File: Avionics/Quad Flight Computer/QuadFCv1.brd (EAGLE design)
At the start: 49.5 x 49.5 mm, 121 parts, among them J2 1050270001, Q1 DMP2035U, Q2 DMP2035U, Q3 DMP2035U, SW1 2-1437565-9, U1 TM4C123GH6PZ, U10 LTC4412, U11 AP7215-33YG-13, U2 74LVC4245APW, U3 ATMEGA32U2-MU, U5 MPU-6000, U6 HMC5883LSMD, U7 MS5611-01BA, U8 74AUP1G19GW, U9 S25FL127S, X1 HWB, Y1 32.768KHZ, Y2 AWSCR-20.00CW-T, Y3 PRQC16.00SR5010X000

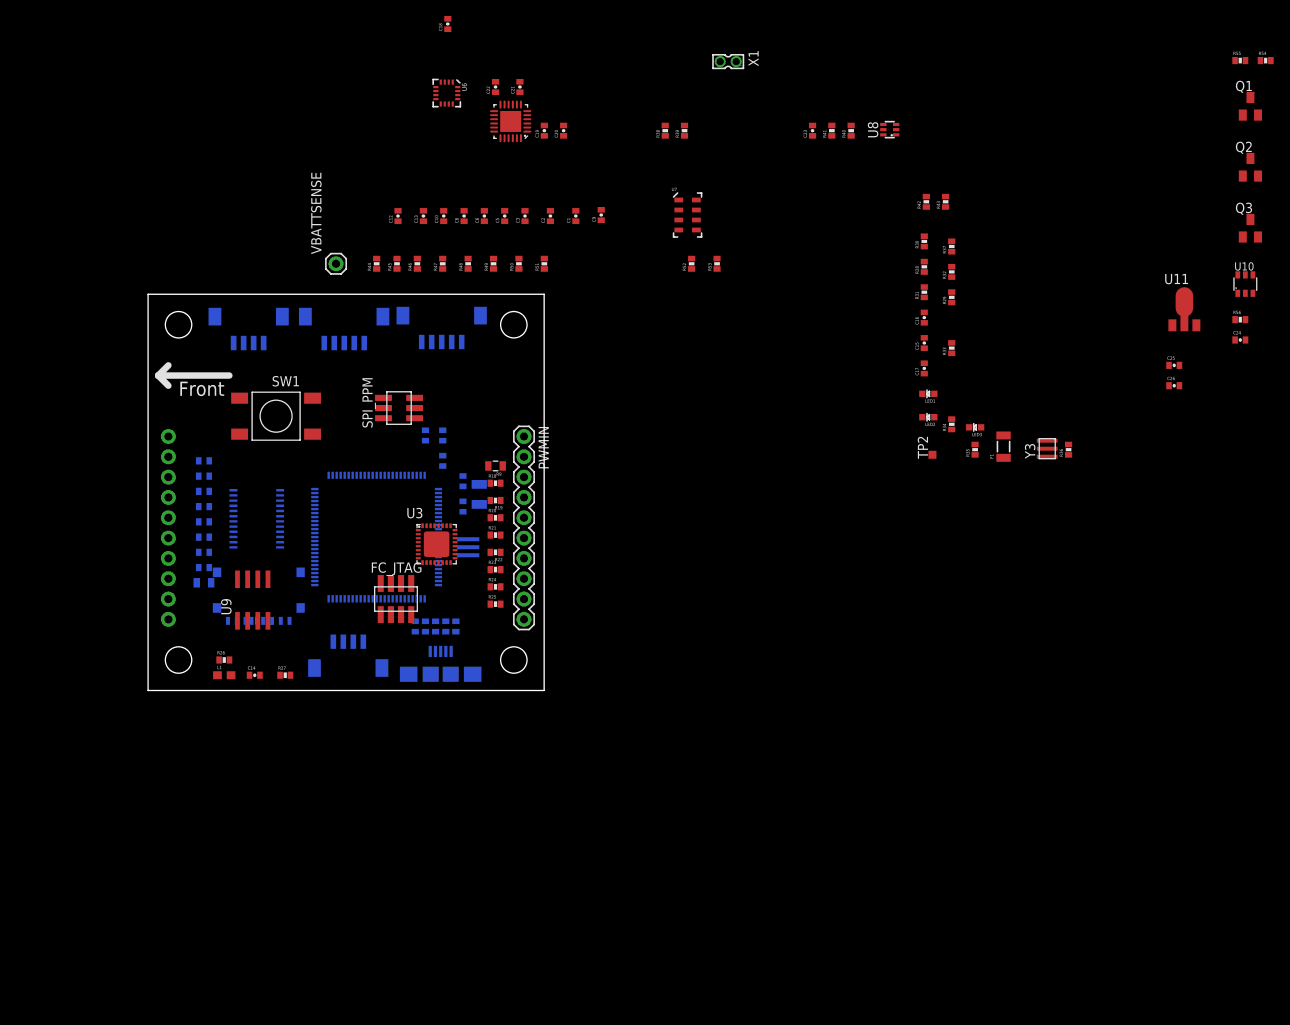
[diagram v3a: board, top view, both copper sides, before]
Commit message: Consolidated entire design into single FC library. Makes everything neater and avoids package conflicts. Using any new package should be added to this library OR copied to it from another lib.
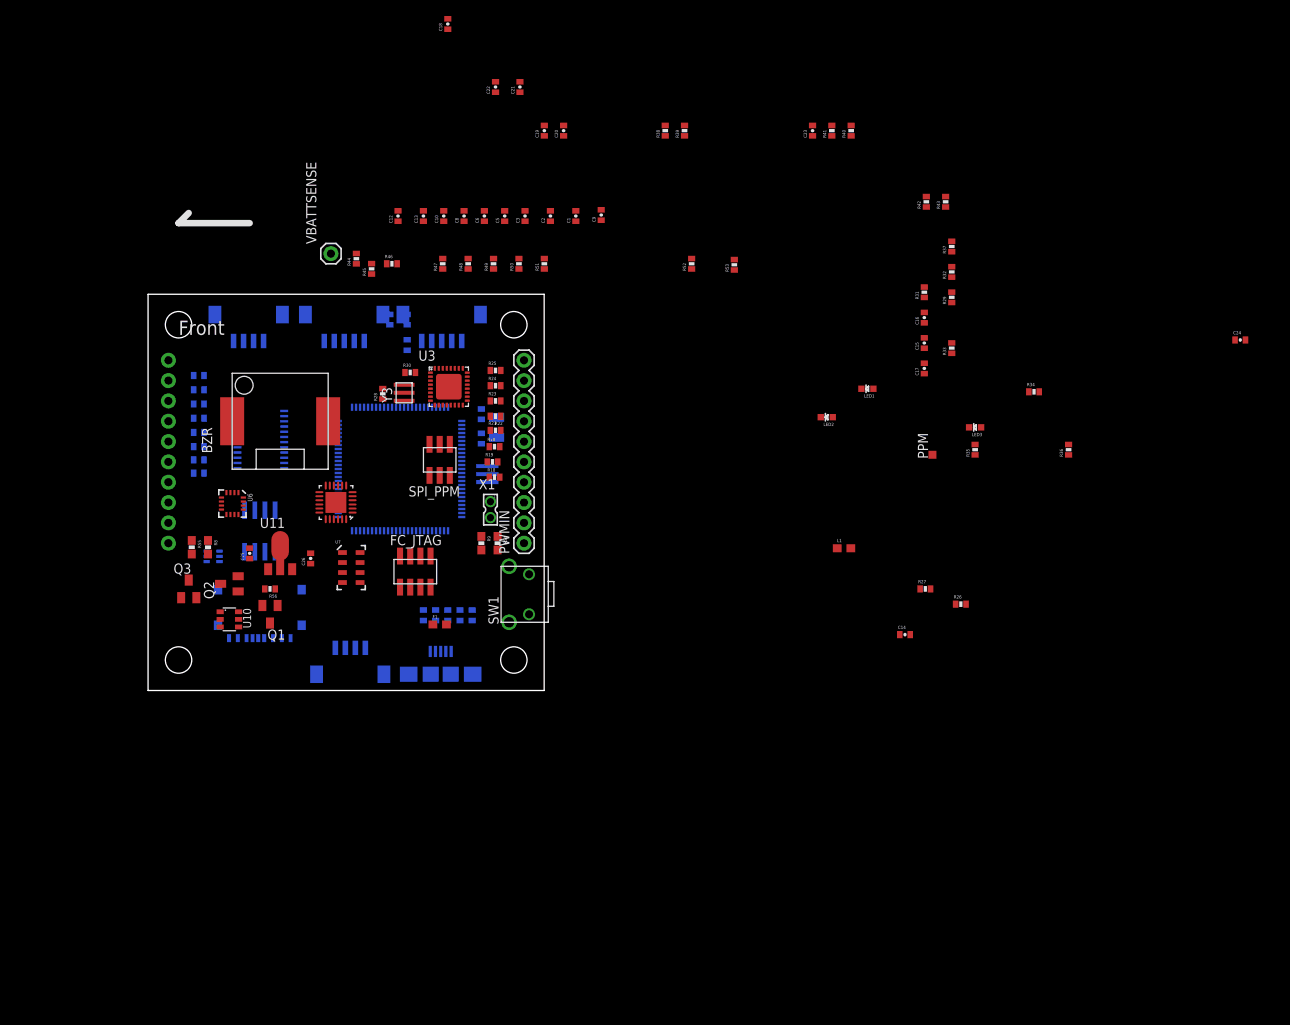
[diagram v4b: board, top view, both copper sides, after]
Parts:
- removed TP2: TPSQTP10SQ, testpad:TP10SQ
- added BZR: CMT-1203-SMT, QuadFCv1:CMT-1203-SMT
- added PPM: TESTPAD_TPSQTP10SQ, QuadFCv1:TP10SQ
- C1, C10, C11, C12, C13, C14, C15, C16, C17, C18, C19, C2, C20, C21, C22, C23, C24, C25, C26, C3, C4, C5, C6, C7, C8, C9: device SparkFun-Capacitors:0402-CAP -> QuadFCv1:0402-CAP
- F1: device SparkFun:PTC-1206 -> QuadFCv1:SPARKFUN_0603
- FC_JTAG: device Shared Libraries:2X4_SMT-0.05 -> QuadFCv1:2X4_SMT-0.05
- GPS, I2C: device Shared Libraries:DF13_4POS -> QuadFCv1:DF13_4POS
- ISENSE, RADIO1: device Shared Libraries:DF13_5POS -> QuadFCv1:DF13_5POS
- J2: device Shared Libraries:1050270001 -> QuadFCv1:1050270001
- L1: device SparkFun-Passives:0603 -> QuadFCv1:0603
- LED1, LED2, LED3: device SparkFun:LED-0603 -> QuadFCv1:SPARKFUN_LED-0603
- PWMIN, PWMOUT: device SparkFun-Connectors:1X10 -> QuadFCv1:1X10
- Q1, Q2, Q3: device Shared Libraries:SOT23 -> QuadFCv1:SOT23
- R1, R10, R11, R12, R13, R14, R15, R16, R17, R18, R19, R2, R20, R21, R22, R23, R24, R25, R26, R27, R28, R29, R3, R30, R31, R32, R33, R34, R35, R36, R37, R38, R39, R4, R40, R41, R42, R43, R44, R45, R46, R47, R48, R49, R5, R50, R51, R52, R53, R6, R7: device SparkFun-Resistors:0402-RES -> QuadFCv1:0402-RES
- R54, R55: device SparkFun-Resistors:0402-RES -> QuadFCv1:0603-RES
- R56: device Shared Libraries:0402-RES -> QuadFCv1:0402-RES
- R8, R9: device SparkFun-Resistors:0805 -> QuadFCv1:0603-RES
- SPI_PPM: device Shared Libraries:2X3_SMT_0.5 -> QuadFCv1:2X3_SMT_0.5
- STANDOFF1, STANDOFF2, STANDOFF3, STANDOFF4: device SparkFun-Electromechanical:STAND-OFF -> QuadFCv1:STAND-OFF
- SW1: value 2-1437565-9 -> PTS635VL31-VERT; device Shared Libraries:SMD_BUTTON_6X6 -> QuadFCv1:PTS635VL31
- U1: device Shared Libraries:LQFP100 -> QuadFCv1:LQFP100
- U10: device Shared Libraries:SOT23-6 -> QuadFCv1:SOT23-6
- U11: device Shared Libraries:SOT89 -> QuadFCv1:SOT89
- U12: device SparkFun-Connectors:USB-AB-MICRO-SMD -> QuadFCv1:USB-AB-MICRO-SMD
- U2: device Shared Libraries:TSSOP24 -> QuadFCv1:TSSOP24
- U3: device atmel:QFN32 -> QuadFCv1:QFN32
- U5: value MPU-6000 -> INVESENSE_MPU-6000; device Invesense:QFN-24-4MM2 -> QuadFCv1:QFN-24-4MM2
- U6: device Shared Libraries:16LPCC -> QuadFCv1:16LPCC
- U7: device 3DRobotics:MS5611-01BA -> QuadFCv1:MS5611-01BA
- U8: device Shared Libraries:SOT363_PHILIPS -> QuadFCv1:SOT363_PHILIPS
- U9: device Shared Libraries:SOIC8 -> QuadFCv1:SOIC8
- VBATTSENSE: device SparkFun-Connectors:1X01 -> QuadFCv1:1X01
- X1: device con-molex:87758-0216 -> QuadFCv1:87758-0216
- Y1: device Shared Libraries:ECS-.327-12.5-34B -> QuadFCv1:ECS-.327-12.5-34B
- Y2: device Shared Libraries:AWSCR-CW -> QuadFCv1:AWSCR-CW
- Y3: device Shared Libraries:PRQC16.00SR5010X000 -> QuadFCv1:PRQC16.00SR5010X000
- moved R55 144.5 mm to (5.46, 17.9), turned to 270 degrees
- moved Q3 140.2 mm to (5.08, 12.7)
- moved Q1 138.0 mm to (15.2, 9.53), turned to 180 degrees
- moved Q2 137.8 mm to (10.2, 13.3), turned to 90 degrees
- moved U10 133.7 mm to (10.2, 8.89), turned to 270 degrees
- moved R56 125.9 mm to (15.2, 12.7), turned to 180 degrees
- moved C25 117.9 mm to (12.7, 17.1), turned to 90 degrees
- moved U11 117.1 mm to (16.5, 17.1)
- moved R54 113.4 mm to (43.7, 18.4), turned to 270 degrees
- moved C26 110.1 mm to (20.3, 16.5), turned to 90 degrees
- moved U8 100.0 mm to (8.13, 16.8), flipped to the bottom, turned to 270 degrees
- moved R26 92.3 mm to (101.6, 10.8)
- moved C14 81.4 mm to (94.6, 6.99)
- moved R27 80.7 mm to (97.2, 12.7)
- moved Y3 80.7 mm to (32.0, 37.2)
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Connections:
- removed net VBUS: F1.2
- net FC_RESET_L: no longer SW1.1
- net GND: now also SW1.1; no longer SW1.3, SW1.4
- net PPM_OUT: now also PPM.TP; no longer TP2.TP
- net VUSB: now also F1.2

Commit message: Finished first attempt to layout EVERYTHING.
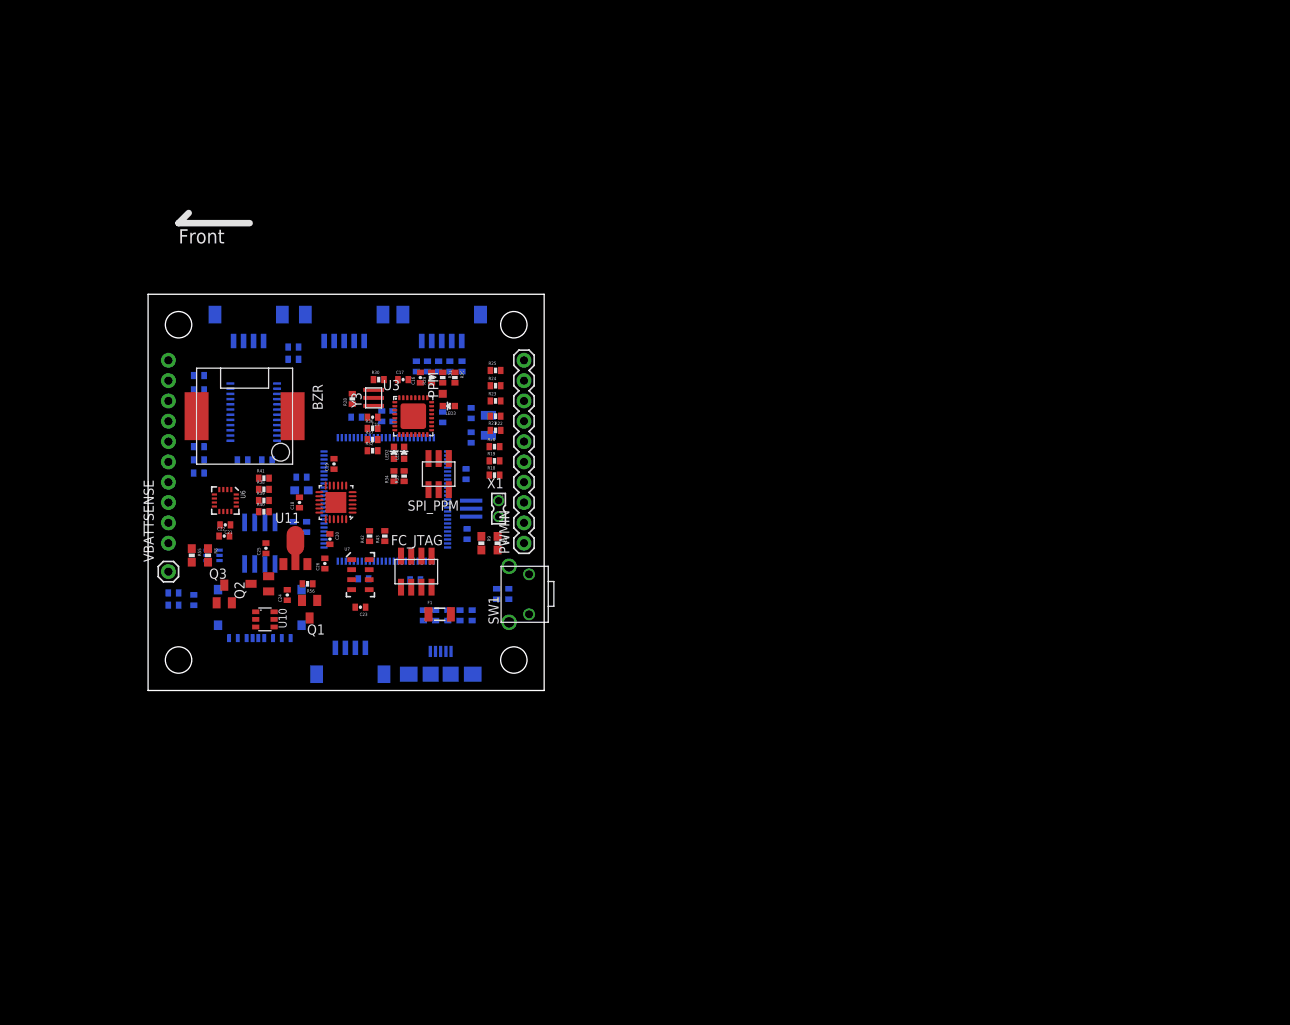
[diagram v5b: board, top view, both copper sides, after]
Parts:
- F1: device QuadFCv1:SPARKFUN_0603 -> QuadFCv1:PTC-1206
- moved C24 123.3 mm to (17.4, 11.9), turned to 90 degrees
- moved R26 88.6 mm to (14.9, 28.8), flipped to the bottom
- moved R40 87.5 mm to (14.5, 22.4), turned to 0 degrees
- moved R36 87.0 mm to (28.1, 32.8), turned to 0 degrees
- moved R27 86.9 mm to (11.8, 28.8), flipped to the bottom
- moved R41 83.2 mm to (14.5, 26.5), turned to 0 degrees
- moved C23 82.1 mm to (26.5, 10.4), turned to 180 degrees
- moved R43 81.6 mm to (29.6, 19.3)
- moved R42 81.2 mm to (27.7, 19.3)
- moved R34 80.7 mm to (30.7, 26.8), turned to 90 degrees
- moved C14 78.0 mm to (19.2, 26.7), flipped to the bottom, turned to 180 degrees
- moved R37 76.3 mm to (28.1, 31.4), turned to 0 degrees
- moved R32 75.8 mm to (28.1, 30.0), turned to 0 degrees
- moved R33 70.3 mm to (32.0, 26.8)
- moved R39 70.0 mm to (14.5, 23.7), turned to 0 degrees
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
